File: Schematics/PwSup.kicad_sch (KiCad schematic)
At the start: 28 parts, among them J3 Phase, J4 PX Ph, J5 PXB10C, J6 Neutral, J7 Px N, SW2 SW_SPST, U3 TL072, U4 LM317_TO-220

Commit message: Dev(#4)
* Patch 0

PCB updates

* Patch 1

Major PCB update

* Delete AMP-MA-backups directory

* Patch 2 gitignore update

PCB update

* Repository cleaned up

* PCB upd

Traces upd, created net classes

* Beta Version 0.0.1

Traces upd, Readme Upd
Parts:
- J3: value Phase -> Neutral
- J4: value PX Ph -> Px N
- J6: value Neutral -> Phase
- J7: value Px N -> Px Ph
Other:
- moved on the sheet: C18, C19, CE2, CE3, D10, D7, D8, D9, F1, J3, J4, J5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

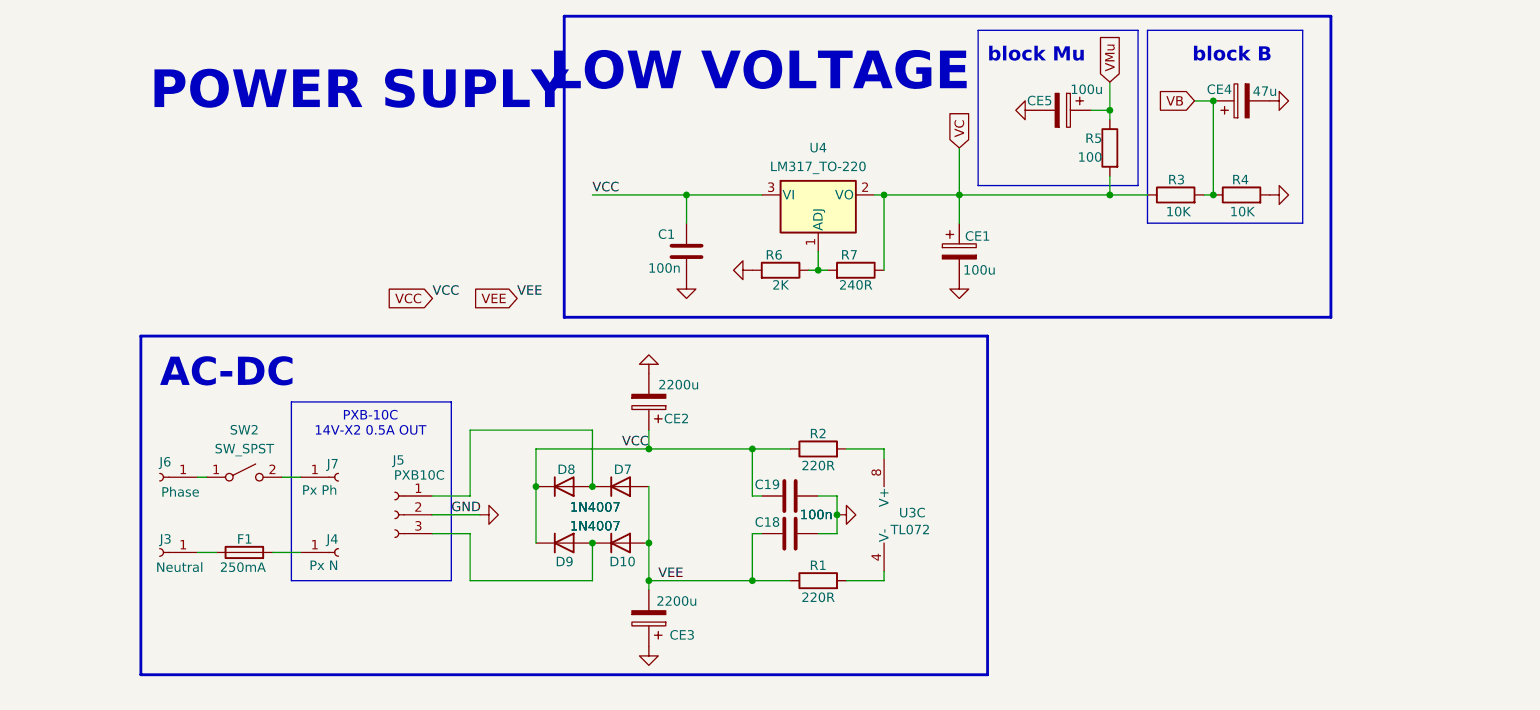
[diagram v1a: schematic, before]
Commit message: feat: start version 0.1.0 development
Schemati upd: Revorked Power supply module
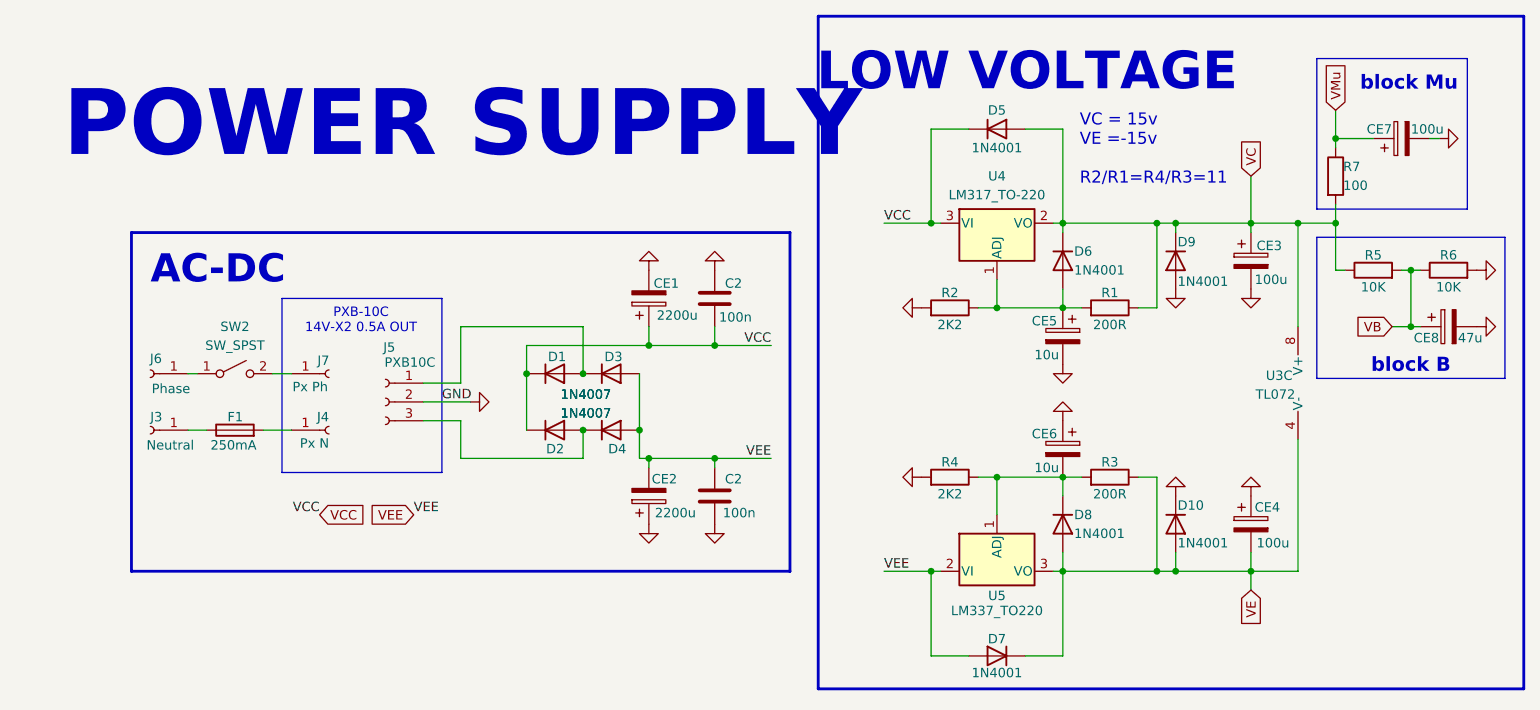
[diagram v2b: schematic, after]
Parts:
- removed C1: 100n, PrLib:C_disc_D7_W2.5_P5, symbol Device:C
- removed R1, R2: 220R, Resistor_THT:R_Axial_DIN0614_L14.3mm_D5.7mm_P20.32mm_Horizontal, symbol Device:R
- added CE4: 100u, Capacitor_THT:CP_Radial_D6.3mm_P2.50mm, symbol Device:C_Polarized
- added CE5, CE6: 10u, Capacitor_THT:CP_Radial_D6.3mm_P2.50mm, symbol Device:C_Polarized
- added D10, D5, D6, D7, D8, D9: 1N4001, Diode_THT:D_DO-41_SOD81_P10.16mm_Horizontal, symbol Diode:1N4001
- added R3: 200R, Resistor_THT:R_Axial_DIN0207_L6.3mm_D2.5mm_P10.16mm_Horizontal, symbol Device:R
- added R4: 2K2, Resistor_THT:R_Axial_DIN0207_L6.3mm_D2.5mm_P10.16mm_Horizontal, symbol Device:R
- added U5: LM337_TO220, Package_TO_SOT_THT:TO-220-3_Horizontal_TabDown, symbol Regulator_Linear:LM337_TO220
- R1: renamed from R7; value 240R -> 200R
- R2: renamed from R6; value 2K -> 2K2
- renumbered C18 to C2, C19 to C2, CE2 to CE1, CE3 to CE2, CE1 to CE3, CE5 to CE7, CE4 to CE8, D8 to D1, D9 to D2, D7 to D3, D10 to D4, R3 to R5, R4 to R6, R5 to R7
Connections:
- net GND: now also CE4.1, CE5.2, CE6.1, D10.1 (K), D9.2 (A), R4.2
- net VC: now also U3.8 (V+), D5.2 (A), D6.1 (K), D9.1 (K)
- net VCC: now also D5.1 (K)
- net VEE: now also D7.2 (A), U5.2 (VI)
- net at R1.2, R2.1, U4.1 (ADJ): now also CE5.1, D6.2 (A)
- net VE: now reaches U3.4 (V-)
- net VE: now also CE4.2, D10.2 (A), D7.1 (K), D8.2 (A), R3.1, U5.3 (VO)
- new net: CE6.2, D8.1 (K), R3.2, R4.1, U5.1 (ADJ)
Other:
- note added: "POWER SUPPLY"
- note added: "VC = 15v VE =-15v R2/R1=R4/R3=11"
- note removed: "POWER SUPLY"
- moved on the sheet: C2, CE1, CE2, CE3, CE7, CE8, D1, D2, D3, D4, F1, J3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

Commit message: Schematic upd
Revorked bypass module, Annotated capacitors, Replaced 2N5484 and j209 with 2SK30A
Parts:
- renumbered C2 to C1
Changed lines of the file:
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@@
 		(in_pos_files yes)
 		(dnp no)
-		(property "Reference" "C2"
+		(property "Reference" "C1"
 			(at 95.25 51.308 0)
 			(show_name no)
@@
 			(project "AMP-MA"
 				(path "/4094031b-a9da-4ac5-aaa1-42b342c92a3e/50fcec93-e12d-4852-998b-ff512e6cbf1d"
-					(reference "C2")
+					(reference "C1")
 					(unit 1)
 				)

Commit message: Schematic upd
Revorked mix module, Bypass upd, Replaced 1N914 with 1N4148
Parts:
- renumbered U3 to U1
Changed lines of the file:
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@@
 		(in_pos_files yes)
 		(dnp no)
-		(property "Reference" "U3"
+		(property "Reference" "U1"
 			(at 168.91 63.754 0)
 			(show_name no)
@@
 			(project "AMP-MA"
 				(path "/4094031b-a9da-4ac5-aaa1-42b342c92a3e/50fcec93-e12d-4852-998b-ff512e6cbf1d"
-					(reference "U3")
+					(reference "U1")
 					(unit 3)
 				)

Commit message: Big Upd
Schemaics: Tone Stack moved to differend file and made some differend variants of, reassigned some footprints

Readme upd: added tone stacks types
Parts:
- R5, R6, R7: footprint Resistor_THT:R_Axial_DIN0207_L6.3mm_D2.5mm_P7.62mm_Horizontal -> Resistor_THT:R_Axial_DIN0207_L6.3mm_D2.5mm_P10.16mm_Horizontal
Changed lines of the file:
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@@
 			)
 		)
-		(property "Footprint" "Resistor_THT:R_Axial_DIN0207_L6.3mm_D2.5mm_P7.62mm_Horizontal"
+		(property "Footprint" "Resistor_THT:R_Axial_DIN0207_L6.3mm_D2.5mm_P10.16mm_Horizontal"
 			(at 191.77 51.308 90)
 			(hide yes)
@@
 			)
 		)
-		(property "Footprint" "Resistor_THT:R_Axial_DIN0207_L6.3mm_D2.5mm_P7.62mm_Horizontal"
+		(property "Footprint" "Resistor_THT:R_Axial_DIN0207_L6.3mm_D2.5mm_P10.16mm_Horizontal"
 			(at 181.61 51.308 90)
 			(hide yes)
@@
 			)
 		)
-		(property "Footprint" "Resistor_THT:R_Axial_DIN0207_L6.3mm_D2.5mm_P7.62mm_Horizontal"
+		(property "Footprint" "Resistor_THT:R_Axial_DIN0207_L6.3mm_D2.5mm_P10.16mm_Horizontal"
 			(at 174.752 36.83 90)
 			(hide yes)

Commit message: Cosmetic upd
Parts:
- removed J3: Neutral, PrLib:connector, symbol Connector:Conn_01x01_Socket
- removed J4: Px N, PrLib:connector, symbol Connector:Conn_01x01_Socket
- removed J5: PXB10C, Connector_JST:JST_XH_B3B-XH-A_1x03_P2.50mm_Vertical, symbol Connector:Conn_01x03_Socket
- removed J6: Phase, symbol Connector:Conn_01x01_Socket
- removed J7: Px Ph, symbol Connector:Conn_01x01_Socket
- added T1: PXB-10C 14V-X2 0.5A OUT, symbol Device:Transformer_1P_2S
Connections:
- net GND: now also T1.4 (SB), T1.5 (SC)
- net PXB_N: now reaches F1.2
- net PXB_N: now also T1.2 (AB)
- net Phase: now reaches SW2.1 (A)
- net PXB_3: now reaches D1.2 (A), D3.1 (K)
- net PXB_3: now also T1.3 (SA)
- net PXB_1: now reaches D2.2 (A), D4.1 (K)
- net PXB_1: now also T1.6 (SD)
- net PXB_Ph: now reaches SW2.2 (B)
- net PXB_Ph: now also T1.1 (AA)
- net Neutral: now reaches F1.1
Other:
- note removed: "PXB-10C 14V-X2 0.5A OUT"
- note removed: "VC = 15v VE =-15v R2/R1=R4/R3=11"
- moved on the sheet: CE3, CE4, CE5, CE6, CE7, CE8, D10, D5, D6, D7, D8, D9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

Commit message: Version 0.1.0 Pre-Release
Reworked PCB, reanotated some components, changed some footprints
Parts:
- CE1, CE2: footprint Capacitor_THT:CP_Radial_D14.0mm_P7.50mm -> Capacitor_THT:CP_Radial_D16.0mm_P7.50mm
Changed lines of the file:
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@@
 			)
 		)
-		(property "Footprint" "Capacitor_THT:CP_Radial_D14.0mm_P7.50mm"
+		(property "Footprint" "Capacitor_THT:CP_Radial_D16.0mm_P7.50mm"
 			(at 84.7852 49.53 0)
 			(hide yes)
@@
 			)
 		)
-		(property "Footprint" "Capacitor_THT:CP_Radial_D14.0mm_P7.50mm"
+		(property "Footprint" "Capacitor_THT:CP_Radial_D16.0mm_P7.50mm"
 			(at 84.7852 76.2 0)
 			(hide yes)

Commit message: Version 0.1.0 Release
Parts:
- U4: value LM317_TO-220 -> LM317
- U5: value LM337_TO220 -> LM337
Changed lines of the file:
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@@
 			)
 		)
-		(property "Value" "LM337_TO220"
+		(property "Value" "LM337"
 			(at 129.54 95.504 0)
 			(show_name no)
@@
 			)
 		)
-		(property "Value" "LM317_TO-220"
+		(property "Value" "LM317"
 			(at 129.54 39.37 0)
 			(show_name no)
